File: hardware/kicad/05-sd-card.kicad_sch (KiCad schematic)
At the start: 1 part, among them U6 SD_Card_SPI

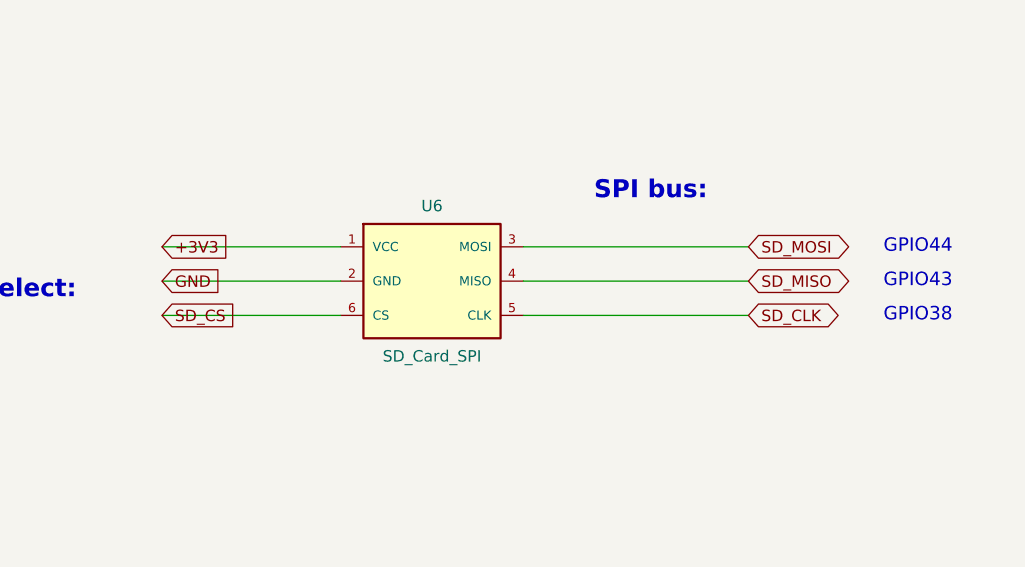
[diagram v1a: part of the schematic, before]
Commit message: feat(containment): layer 6 — ERC warning burn-down, 676 to ZERO, gate at all severities
Three root causes, three fixes in the schematic generator:

- 507 endpoint_off_grid: sheets lay out on a human 1 mm grid while KiCad
  connects on 1.27 mm. snap() in kicad_primitives now grid-snaps every
  connection-bearing coordinate at emission. Snapping is monotonic and
  distributes over the library's grid-multiple pin offsets, so points
  that coincided before still coincide after; zero-length stub wires
  that collapse onto their anchor are dropped.
- The stragglers came from three symbols whose pin connection points
  were themselves off-grid: BAT54C (±5.0 → ±5.08, top 5.0 → 5.08, used
  by D1 and Q1), USBLC6-2SC6 (±10.0 → ±10.16), Speaker (±0.635 →
  ±1.27). Their sheet wiring moved with them in the same commit.
- 169 lib_symbol_issues: bare lib_ids referenced library "" which no
  configuration includes. Symbols are now emu:<name>, resolved by a
  generated hardware/kicad/sym-lib-table + emu.kicad_sym built from the
  same SYMBOLS strings as the embedded caches — cache and library
  cannot disagree by construction.

verify_erc now runs --severity-all against a ZERO baseline: from zero,
any new warning is a regression a specific change introduced. The
website's per-sheet SVGs/PDFs are re-rendered, and the "Download all
sheets" PDF — a one-off hand merge nothing regenerated, stale since the
R25 respin — is now merged by render-schematics.sh from the exported
sheets.

Suite: 85/85 green; netlist_diff vs PCB confirms connectivity unchanged.

Co-Authored-By: Claude Fable 5 <noreply@anthropic.com>
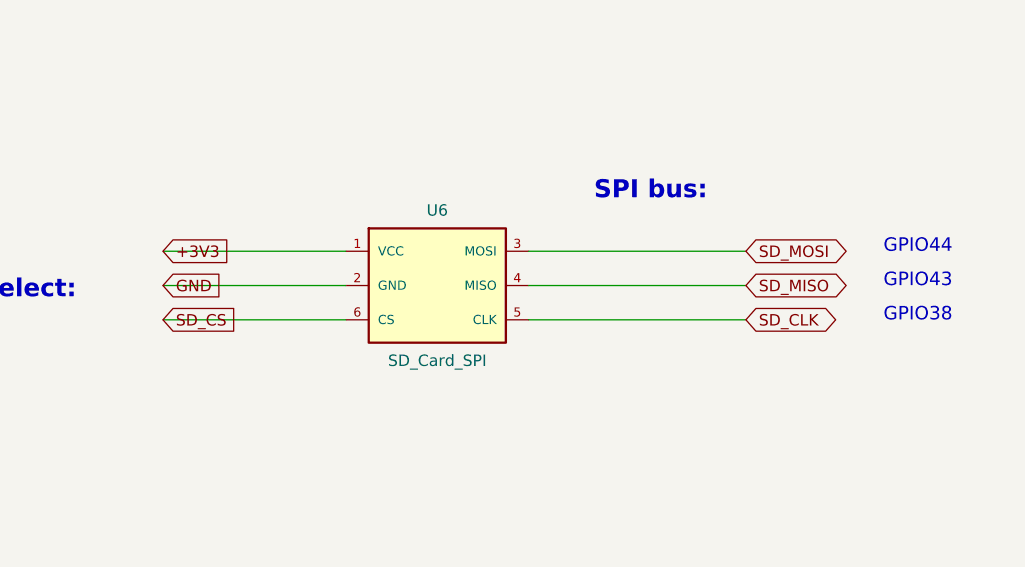
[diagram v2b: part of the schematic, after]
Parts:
- U6: symbol SD_Module -> emu:SD_Module
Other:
- moved on the sheet: U6
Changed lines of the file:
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@@
   (text "STORAGE - Micro SD Card" (at 30 25 0) (effects (font (size 5 5) bold) (justify left)))
   (text "SPI interface for ROM storage (SNES ROMs up to 6MB)" (at 30 33 0) (effects (font (size 2.54 2.54)) (justify left)))
-  (symbol (lib_id "SD_Module") (at 148 110 0) (unit 1) (exclude_from_sim no) (in_bom yes) (on_board yes) (dnp no) (property "Reference" "U6" (at 148 101.65 0) (effects (font (size 1.27 1.27)))) (property "Value" "SD_Card_SPI" (at 148 118.35 0) (effects (font (size 1.27 1.27)))) (pin "1") (pin "2") (pin "3") (pin "4") (pin "5") (pin "6") (instances (project "esp32-emu-turbo" (path "/00000006-cafe-4000-8000-000000000006" (reference "U6") (unit 1)) (path "/00000001-cafe-4000-8000-000000000001/00000006-cafe-4000-8000-000000000006" (reference "U6") (unit 1)))))
-  (global_label "+3V3" (shape input) (at 118 106.19 0) (effects (font (size 1.27 1.27))) (property "Intersheetrefs" "" (at 0 0 0) (effects (font (size 1.27 1.27)) hide)))
-  (wire (pts (xy 118 106.19) (xy 137.84 106.19)) (stroke (width 0) (type default)))
-  (global_label "GND" (shape input) (at 118 110 0) (effects (font (size 1.27 1.27))) (property "Intersheetrefs" "" (at 0 0 0) (effects (font (size 1.27 1.27)) hide)))
-  (wire (pts (xy 118 110) (xy 137.84 110)) (stroke (width 0) (type default)))
+  (symbol (lib_id "emu:SD_Module") (at 148.59 110.49 0) (unit 1) (exclude_from_sim no) (in_bom yes) (on_board yes) (dnp no) (property "Reference" "U6" (at 148.59 102.14 0) (effects (font (size 1.27 1.27)))) (property "Value" "SD_Card_SPI" (at 148.59 118.83999999999999 0) (effects (font (size 1.27 1.27)))) (pin "1") (pin "2") (pin "3") (pin "4") (pin "5") (pin "6") (instances (project "esp32-emu-turbo" (path "/00000006-cafe-4000-8000-000000000006" (reference "U6") (unit 1)) (path "/00000001-cafe-4000-8000-000000000001/00000006-cafe-4000-8000-000000000006" (reference "U6") (unit 1)))))
+  (global_label "+3V3" (shape input) (at 118.11 106.68 0) (effects (font (size 1.27 1.27))) (property "Intersheetrefs" "" (at 0 0 0) (effects (font (size 1.27 1.27)) hide)))
+  (wire (pts (xy 118.11 106.68) (xy 138.43 106.68)) (stroke (width 0) (type default)))
+  (global_label "GND" (shape input) (at 118.11 110.49 0) (effects (font (size 1.27 1.27))) (property "Intersheetrefs" "" (at 0 0 0) (effects (font (size 1.27 1.27)) hide)))
+  (wire (pts (xy 118.11 110.49) (xy 138.43 110.49)) (stroke (width 0) (type default)))
   (text "SPI bus:" (at 166 100 0) (effects (font (size 2 2) bold) (justify left)))
-  (wire (pts (xy 158.16 106.19) (xy 183.16 106.19)) (stroke (width 0) (type default)))
-  (global_label "SD_MOSI" (shape bidirectional) (at 183.16 106.19 0) (effects (font (size 1.27 1.27))) (property "Intersheetrefs" "" (at 0 0 0) (effects (font (size 1.27 1.27)) hide)))
+  (wire (pts (xy 158.75 106.68) (xy 182.88 106.68)) (stroke (width 0) (type default)))
+  (global_label "SD_MOSI" (shape bidirectional) (at 182.88 106.68 0) (effects (font (size 1.27 1.27))) (property "Intersheetrefs" "" (at 0 0 0) (effects (font (size 1.27 1.27)) hide)))
   (text "GPIO44" (at 198.16 106.19 0) (effects (font (size 1.5 1.5)) (justify left)))
-  (wire (pts (xy 158.16 110) (xy 183.16 110)) (stroke (width 0) (type default)))
-  (global_label "SD_MISO" (shape bidirectional) (at 183.16 110 0) (effects (font (size 1.27 1.27))) (property "Intersheetrefs" "" (at 0 0 0) (effects (font (size 1.27 1.27)) hide)))
+  (wire (pts (xy 158.75 110.49) (xy 182.88 110.49)) (stroke (width 0) (type default)))
+  (global_label "SD_MISO" (shape bidirectional) (at 182.88 110.49 0) (effects (font (size 1.27 1.27))) (property "Intersheetrefs" "" (at 0 0 0) (effects (font (size 1.27 1.27)) hide)))
   (text "GPIO43" (at 198.16 110 0) (effects (font (size 1.5 1.5)) (justify left)))
-  (wire (pts (xy 158.16 113.81) (xy 183.16 113.81)) (stroke (width 0) (type default)))
-  (global_label "SD_CLK" (shape bidirectional) (at 183.16 113.81 0) (effects (font (size 1.27 1.27))) (property "Intersheetrefs" "" (at 0 0 0) (effects (font (size 1.27 1.27)) hide)))
+  (wire (pts (xy 158.75 114.3) (xy 182.88 114.3)) (stroke (width 0) (type default)))
+  (global_label "SD_CLK" (shape bidirectional) (at 182.88 114.3 0) (effects (font (size 1.27 1.27))) (property "Intersheetrefs" "" (at 0 0 0) (effects (font (size 1.27 1.27)) hide)))
   (text "GPIO38" (at 198.16 113.81 0) (effects (font (size 1.5 1.5)) (justify left)))
   (text "Chip Select:" (at 90 111 0) (effects (font (size 2 2) bold) (justify left)))
-  (global_label "SD_CS" (shape input) (at 118 113.81 0) (effects (font (size 1.27 1.27))) (property "Intersheetrefs" "" (at 0 0 0) (effects (font (size 1.27 1.27)) hide)))
-  (wire (pts (xy 118 113.81) (xy 137.84 113.81)) (stroke (width 0) (type default)))
+  (global_label "SD_CS" (shape input) (at 118.11 114.3 0) (effects (font (size 1.27 1.27))) (property "Intersheetrefs" "" (at 0 0 0) (effects (font (size 1.27 1.27)) hide)))
+  (wire (pts (xy 118.11 114.3) (xy 138.43 114.3)) (stroke (width 0) (type default)))
   (text "GPIO39" (at 90 115 0) (effects (font (size 1.5 1.5)) (justify left)))
   (text "Design Notes:" (at 30 160 0) (effects (font (size 2.54 2.54) bold) (justify left)))

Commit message: schematic: zero rendered text overlaps + real P-MOSFET artwork for Q1/Q2
The rendered sheets carried 75 text-on-text collisions the overlap gate
could not see: its model missed pin-number digits, KiCad's mirrored
field justification on 180-degree symbols, and global-label extents.
Root fixes in the generator:

- symbol() now places Reference/Value per part class: beside the body
  for two-pin verticals (R/C/L/Battery), stacked above for LEDs and the
  big ICs whose bottom pin numbers the old centred Value printed over,
  with per-call overrides where a zone is tight. On 180-rotated symbols
  the emitted justification is pre-mirrored, because KiCad flips it.
- Q1/Q2 get PMOS_SOT23 — same pin coordinates as the BAT54C symbol they
  were drawn with (wires and netlist untouched), but the artwork is now
  a P-MOSFET instead of a dual Schottky diode.
- Sheet-level relayouts: decoupling row on 02 spread to 11 mm pitch,
  menu-combo D1 zone on 06, FPC header on 03, PAM bias notes on 04,
  IP5306 KEY exit and the whole power-switch zone on 01.
- ESP32 module pin 41 name blanked — two "GND"s 2.54 mm apart printed
  into each other; number, type and net unchanged.

New gate: verify_schematic_render_overlaps.py exports each sheet to SVG
via kicad-cli and fails if any two DRAWN text runs intersect — ground
truth instead of a re-derived model (47 hits on the old sheet 01, 0
now). Wired into verify-all; dispatch mutation tests 14/14.

Netlist invariance: verify_netlist_diff 4/4, ERC clean at every
severity, schematic-PCB sync green. Website SVG/PDF re-rendered.

Co-Authored-By: Claude Fable 5 <noreply@anthropic.com>
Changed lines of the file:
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@@
   (text "STORAGE - Micro SD Card" (at 30 25 0) (effects (font (size 5 5) bold) (justify left)))
   (text "SPI interface for ROM storage (SNES ROMs up to 6MB)" (at 30 33 0) (effects (font (size 2.54 2.54)) (justify left)))
-  (symbol (lib_id "emu:SD_Module") (at 148.59 110.49 0) (unit 1) (exclude_from_sim no) (in_bom yes) (on_board yes) (dnp no) (property "Reference" "U6" (at 148.59 102.14 0) (effects (font (size 1.27 1.27)))) (property "Value" "SD_Card_SPI" (at 148.59 118.83999999999999 0) (effects (font (size 1.27 1.27)))) (pin "1") (pin "2") (pin "3") (pin "4") (pin "5") (pin "6") (instances (project "esp32-emu-turbo" (path "/00000006-cafe-4000-8000-000000000006" (reference "U6") (unit 1)) (path "/00000001-cafe-4000-8000-000000000001/00000006-cafe-4000-8000-000000000006" (reference "U6") (unit 1)))))
+  (symbol (lib_id "emu:SD_Module") (at 148.59 110.49 0) (unit 1) (exclude_from_sim no) (in_bom yes) (on_board yes) (dnp no) (property "Reference" "U6" (at 148.59 102.14 0) (effects (font (size 1.27 1.27)))) (property "Value" "SD_Card_SPI" (at 148.59 118.84 0) (effects (font (size 1.27 1.27)))) (pin "1") (pin "2") (pin "3") (pin "4") (pin "5") (pin "6") (instances (project "esp32-emu-turbo" (path "/00000006-cafe-4000-8000-000000000006" (reference "U6") (unit 1)) (path "/00000001-cafe-4000-8000-000000000001/00000006-cafe-4000-8000-000000000006" (reference "U6") (unit 1)))))
   (global_label "+3V3" (shape input) (at 118.11 106.68 0) (effects (font (size 1.27 1.27))) (property "Intersheetrefs" "" (at 0 0 0) (effects (font (size 1.27 1.27)) hide)))
   (wire (pts (xy 118.11 106.68) (xy 138.43 106.68)) (stroke (width 0) (type default)))
